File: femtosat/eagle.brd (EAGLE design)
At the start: 24.1 x 63.5 mm, 23 parts, among them U1 ATMEGA328P_TQFP, U2 915MHz, U3 3.3V/150mA, U4 9DoF IMU, U5 BME280, Y1 16MHz

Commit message: PCB before Trace Ripup
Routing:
- net 3.3V: track 140.3 -> 136.8 mm
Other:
- board size 24.1 x 63.5 mm -> 20.3 x 63.5 mm
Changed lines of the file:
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@@
 <board>
 <plain>
-<wire x1="22.86" y1="66.04" x2="22.86" y2="15.24" width="0.1524" layer="20"/>
-<wire x1="-1.27" y1="64.77" x2="-1.27" y2="15.24" width="0.1524" layer="20"/>
-<wire x1="-1.27" y1="15.24" x2="2.54" y2="11.43" width="0.1524" layer="20"/>
-<wire x1="2.54" y1="11.43" x2="19.05" y2="11.43" width="0.1524" layer="20"/>
-<wire x1="19.05" y1="11.43" x2="22.86" y2="15.24" width="0.1524" layer="20"/>
 <text x="5.842" y="64.897" size="1.778" layer="1" font="vector">Angstrom</text>
 <text x="19.431" y="51.562" size="1.016" layer="1" font="vector">SCL</text>
 <text x="19.304" y="49.149" size="1.016" layer="1" font="vector">SDA</text>
-<wire x1="-1.27" y1="64.77" x2="6.35" y2="74.93" width="0.1524" layer="20"/>
-<wire x1="6.35" y1="74.93" x2="15.24" y2="74.93" width="0.1524" layer="20"/>
-<wire x1="15.24" y1="74.93" x2="22.86" y2="66.04" width="0.1524" layer="20"/>
-<hole x="10.668" y="70.485" drill="4.9784"/>
+<wire x1="0" y1="12.7" x2="0" y2="76.2" width="0.254" layer="20"/>
+<wire x1="0" y1="76.2" x2="20.32" y2="76.2" width="0.254" layer="20"/>
+<wire x1="20.32" y1="76.2" x2="20.32" y2="12.7" width="0.254" layer="20"/>
+<wire x1="20.32" y1="12.7" x2="0" y2="12.7" width="0.254" layer="20"/>
 </plain>
 <attributes>
@@
 <wire x1="14.9352" y1="61.722" x2="11.8872" y2="61.722" width="0.254" layer="1"/>
 <wire x1="16.6116" y1="60.0456" x2="14.9352" y2="61.722" width="0.254" layer="1"/>
-<wire x1="16.6116" y1="56.5404" x2="16.6116" y2="60.0456" width="0.254" layer="1"/>
 <wire x1="12.6492" y1="52.578" x2="16.6116" y2="56.5404" width="0.254" layer="1"/>
 <wire x1="2.1336" y1="44.6532" x2="1.9812" y2="44.6532" width="0.254" layer="1"/>
@@
 <wire x1="2.7432" y1="23.1648" x2="2.66" y2="23.13" width="0.254" layer="1"/>
 <wire x1="1.2192" y1="40.0812" x2="1.27" y2="40.22" width="0.254" layer="1"/>
+<wire x1="16.6116" y1="60.0456" x2="16.6116" y2="56.5404" width="0" layer="19" extent="1-1"/>
 </signal>
 <signal name="INT">

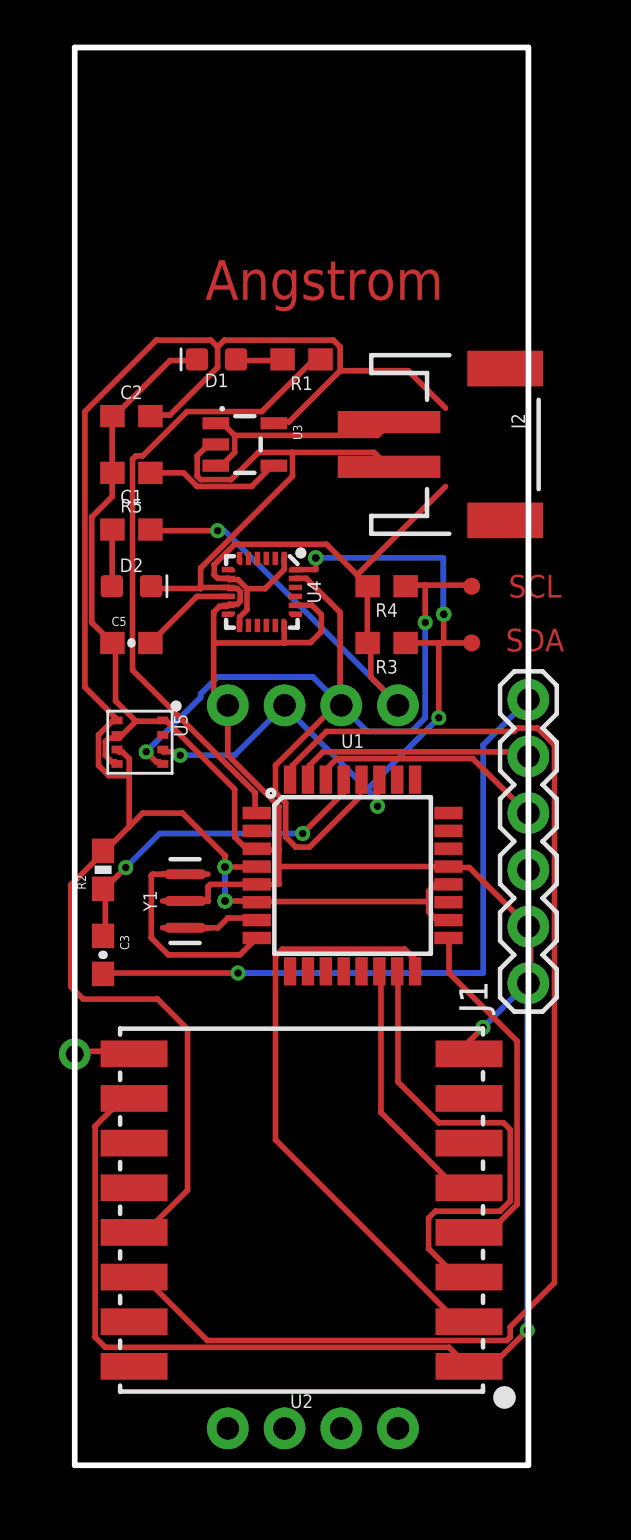
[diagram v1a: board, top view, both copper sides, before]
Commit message: Redesigned to fit Checklist
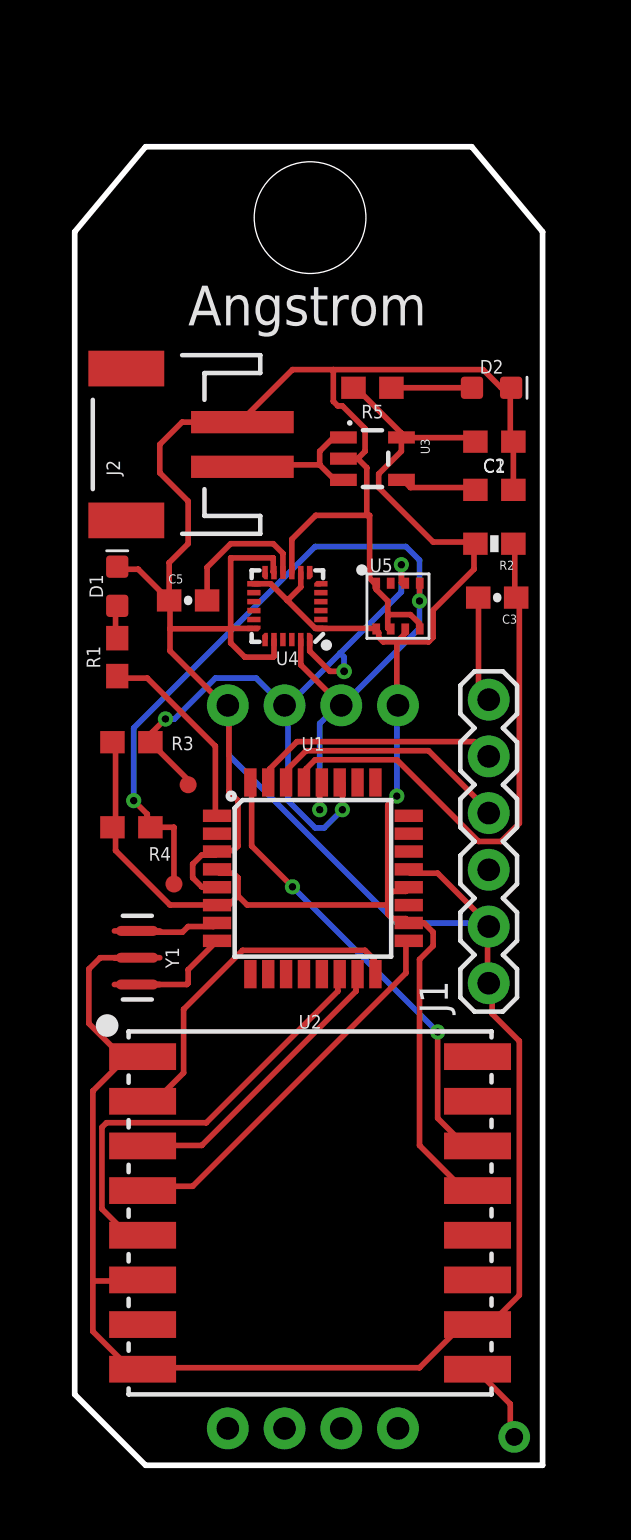
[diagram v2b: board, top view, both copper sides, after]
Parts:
- moved ANT1 26.1 mm to (19.7, 14.0)
- moved C3 23.8 mm to (18.9, 51.6), turned to 180 degrees
- moved R2 22.8 mm to (18.8, 54.0), turned to 180 degrees
- moved TP1 18.9 mm to (4.45, 38.7)
- moved D2 18.4 mm to (18.7, 61.0)
- moved C2 16.3 mm to (18.8, 58.5), turned to 180 degrees
- moved C1 16.3 mm to (18.8, 56.4), turned to 0 degrees
- moved R4 15.7 mm to (2.54, 41.3)
- moved R1 15.7 mm to (1.91, 48.9), turned to 90 degrees
- moved TP2 14.2 mm to (5.08, 43.2)
- moved J2 14.0 mm to (3.81, 58.4), turned to 90 degrees
- moved U5 13.1 mm to (14.5, 51.2), turned to 0 degrees
- moved R5 12.5 mm to (13.3, 61.0), turned to 180 degrees
- moved R3 12.3 mm to (2.54, 45.1)
- moved D1 11.1 mm to (1.91, 52.1), turned to 90 degrees
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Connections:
- net GND: now also U2.6
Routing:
- net 3.3V: track 136.8 -> 81.0 mm, vias 3 -> 1
- net INT: track 58.9 -> 20.8 mm, vias 0 -> 2
- net N$15: track 30.1 -> 4.75 mm, vias 1 -> 0
- net N$13: track 28.4 -> 8.84 mm
- net GND: track 151.5 -> 166.8 mm, vias 2 -> 0
- net N$1: track 27.4 -> 15.7 mm
- net N$14: track 15.4 -> 24.9 mm, vias 2 -> 0
- net N$3: track 21.7 -> 13.2 mm
- net N$6: track 11.7 -> 19.8 mm
- net N$11: track 9.69 -> 4.75 mm
- net SDA: track 35.8 -> 32.2 mm, vias 5 -> 4
- net N$4: track 10.1 -> 6.81 mm
- net N$9: track 6.16 -> 3.50 mm
- net N$18: track 4.36 -> 6.36 mm
- net N$2: track 15.9 -> 17.5 mm
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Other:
- board size 20.3 x 63.5 mm -> 21 x 59.1 mm

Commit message: Added Gnd Pour
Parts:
- moved TP2 0.63 mm to (4.45, 43.2)
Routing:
- added copper zone on layer 1, net GND
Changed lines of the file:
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@@
 <wire x1="20.955" y1="67.945" x2="20.955" y2="12.7" width="0.254" layer="20"/>
 <hole x="10.541" y="68.58" drill="5.0038"/>
-<text x="0.635" y="38.1" size="1.27" layer="23">SCL</text>
-<text x="0.635" y="42.545" size="1.27" layer="23">SDA</text>
 <text x="5.08" y="63.754" size="1.778" layer="21" font="fixed">Angstrom</text>
+<text x="0.762" y="42.672" size="1.27" layer="21" font="fixed">SCL</text>
+<text x="0.635" y="38.1" size="1.27" layer="21" font="fixed">SDA</text>
 </plain>
 <attributes>
@@
 </element>
 <element name="TP1" library="femtosat" package="PAD.03X.03" value="TEST-POINT3" x="4.445" y="38.735" smashed="yes"/>
-<element name="TP2" library="femtosat" package="PAD.03X.03" value="TEST-POINT3" x="5.08" y="43.18" smashed="yes"/>
+<element name="TP2" library="femtosat" package="PAD.03X.03" value="TEST-POINT3" x="4.445" y="43.18" smashed="yes"/>
 <element name="U$1" library="femtosat" package="MEM-HEADERS" value="MEM_MODULE" x="14.478" y="46.736" smashed="yes" rot="R180"/>
 <element name="U1" library="femtosat" package="TQFP32-08" value="ATMEGA328P_TQFP" x="10.668" y="38.989" smashed="yes">
@@
 <wire x1="8.925" y1="52.681" x2="8.89" y2="52.716" width="0.254" layer="1"/>
 <wire x1="8.89" y1="52.716" x2="8.89" y2="53.34" width="0.254" layer="1"/>
+<polygon width="0.1524" layer="1" isolate="0.254">
+<vertex x="0" y="15.875"/>
+<vertex x="0" y="67.945"/>
+<vertex x="3.175" y="71.755"/>
+<vertex x="17.78" y="71.755"/>
+<vertex x="20.955" y="67.945"/>
+<vertex x="20.955" y="12.7"/>
+<vertex x="3.175" y="12.7"/>
+</polygon>
 </signal>
 <signal name="N$5">
@@
 <via x="11.9888" y="42.0624" extent="1-16" drill="0.3302"/>
 <via x="4.064" y="46.1264" extent="1-16" drill="0.3302"/>
-<wire x1="3.39" y1="45.085" x2="5.08" y2="43.395" width="0.254" layer="1"/>
-<wire x1="5.08" y1="43.395" x2="5.08" y2="43.18" width="0.254" layer="1"/>
 <wire x1="10.525" y1="49.6285" x2="10.525" y2="49.165" width="0.254" layer="1"/>
 <wire x1="11.43" y1="48.26" x2="12.065" y2="48.26" width="0.254" layer="1"/>
@@
 <wire x1="12.065" y1="48.895" x2="11.8872" y2="49.0728" width="0.254" layer="16"/>
 <wire x1="10.525" y1="49.165" x2="11.43" y2="48.26" width="0.254" layer="1"/>
+<wire x1="3.39" y1="45.085" x2="4.445" y2="43.18" width="0.254" layer="1"/>
 </signal>
 <signal name="SCL">
